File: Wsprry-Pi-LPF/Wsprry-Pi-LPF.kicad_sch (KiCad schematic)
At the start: 13 parts, among them J1 Conn_01x04, J2 Conn_01x04

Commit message: Add 2m LPF values and resolve ERC findings
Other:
- note added: "External equipment supplies GND"
- note added: "VDRN_FEED"
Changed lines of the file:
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@@
+	)
+	(junction
+		(at 105.41 104.14)
+		(diameter 0)
+		(color 0 0 0 0)
 	)
 	(junction
@@
 	(wire
 		(pts
+			(xy 101.6 104.14) (xy 105.41 104.14)
+		)
+		(stroke
+			(width 0)
+			(type default)
+		)
+	)
+	(wire
+		(pts
 			(xy 115.57 90.17) (xy 120.65 90.17)
 		)
@@
 		(pts
 			(xy 135.89 91.44) (xy 135.89 90.17)
-		)
-		(stroke
-			(width 0)
-			(type default)
-		)
-	)
-	(wire
-		(pts
-			(xy 93.98 107.95) (xy 105.41 107.95)
 		)
 		(stroke
@@
 		)
 	)
-	(label "VDRN_FEED"
-		(at 93.98 107.95 0)
+	(text "VDRN_FEED"
+		(exclude_from_sim no)
+		(at 93.98 105.41 0)
 		(effects
 			(font
 				(size 1.27 1.27)
 			)
-			(justify left bottom)
+		)
+	)
+	(text "External equipment supplies GND"
+		(exclude_from_sim no)
+		(at 81.28 100.33 0)
+		(effects
+			(font
+				(size 1.27 1.27)
+			)
 		)
 	)
@@
 					(unit 1)
 				)
+			)
+		)
+	)
+	(symbol
+		(lib_id "Wsprry Pi LPF:PWR_FLAG")
+		(at 101.6 104.14 180)
+		(unit 1)
+		(body_style 1)
+		(exclude_from_sim no)
+		(in_bom yes)
+		(on_board yes)
+		(in_pos_files yes)
+		(dnp no)
+		(property "Reference" "#FLG01"
+			(at 101.6 106.045 0)
+			(show_name no)
+			(do_not_autoplace no)
+			(hide yes)
+			(effects
+				(font
+					(size 1.27 1.27)
+				)
+			)
+		)
+		(property "Value" "PWR_FLAG"
+			(at 101.6 107.95 0)
+			(show_name no)
+			(do_not_autoplace no)
+			(hide yes)
+			(effects
+				(font
+					(size 1.27 1.27)
+				)
+			)
+		)
+		(property "Footprint" ""
+			(at 101.6 104.14 0)
+			(show_name no)
+			(do_not_autoplace no)
+			(hide yes)
+			(effects
+				(font
+					(size 1.27 1.27)
+				)
+			)
+		)
+		(property "Datasheet" ""
+			(at 101.6 104.14 0)
+			(show_name no)
+			(do_not_autoplace no)
+			(hide yes)
+			(effects
+				(font
+					(size 1.27 1.27)
+				)
+			)
+		)
+		(property "Description" "Special symbol for telling ERC where power comes from"
+			(at 101.6 104.14 0)
+			(show_name no)
+			(do_not_autoplace no)
+			(hide yes)
+			(effects
+				(font
+					(size 1.27 1.27)
+				)
+			)
+		)
+		(pin "1"
+		)
+		(instances
+			(project "Wsprry-Pi-LPF"
+				(path "/a5c3480f-f07b-4318-b0ac-3cbcb5b2943e"
+					(reference "#FLG01")
+					(unit 1)
+				)

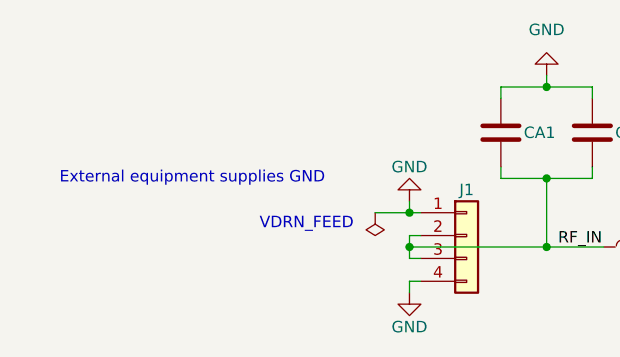
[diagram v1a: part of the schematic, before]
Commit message: Document current LPF validation and 2m values
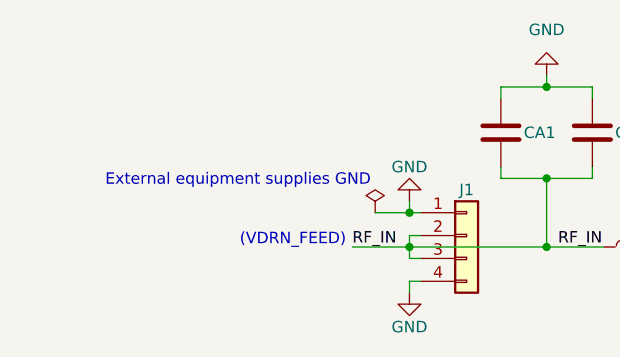
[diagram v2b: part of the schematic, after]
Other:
- note added: "(VDRN_FEED)"
- note removed: "VDRN_FEED"

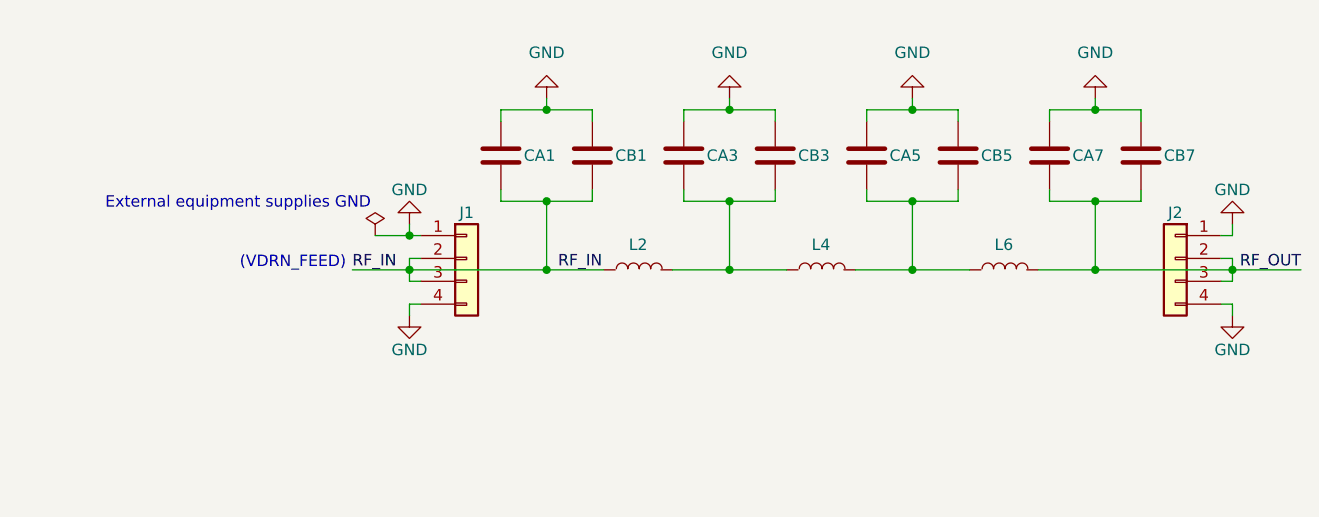
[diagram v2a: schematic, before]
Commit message: Header changed to match QRP Labs
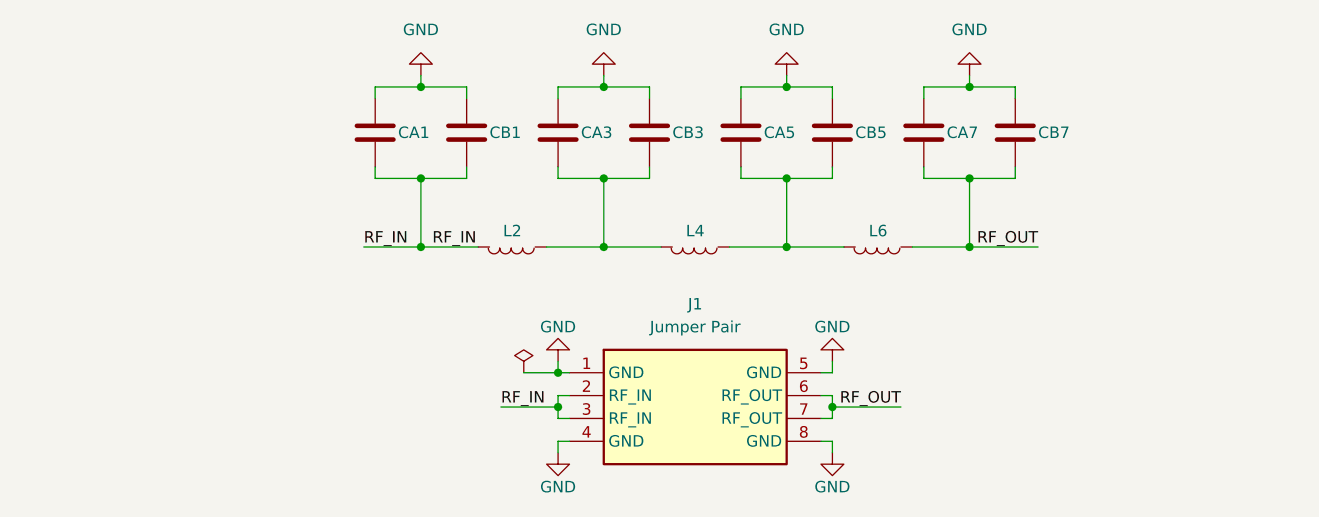
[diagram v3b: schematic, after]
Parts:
- removed J1, J2: Conn_01x04, Wsprry Pi LPF:PinHeader_1x04_P2.54mm_Vertical, symbol Wsprry Pi LPF:Conn_01x04
- added J1: Jumper Pair, Wsprry Pi LPF:LPF_HeaderPair_2x1x04_P2.54mm_S33.02mm, symbol Wsprry Pi LPF:LPF_HeaderPair_2x1x04_P2.54mm_S33.02mm
- renumbered CB7 to CA1, CB1 to CA7, CA7 to CB1, CA1 to CB7, L6 to L2, L2 to L6
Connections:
- net GND: now also J1.1 (GND), J1.4 (GND), J1.5 (GND), J1.8 (GND)
- net RF_IN: now also CA1.2, CB1.2, L2.2, J1.2 (RF_IN), J1.3 (RF_IN); no longer CA7.2, CB7.2, L6.1
- net RF_OUT: now also CA7.2, CB7.2, L6.1, J1.6 (RF_OUT), J1.7 (RF_OUT); no longer CA1.2, CB1.2, L2.2
- net at CA5.2, CB5.2: now also L4.1, L6.2; no longer L2.1, L4.2
- net at CA3.2, CB3.2: now also L2.1, L4.2; no longer L4.1, L6.2
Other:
- note removed: "(VDRN_FEED)"
- note removed: "External equipment supplies GND"
- moved on the sheet: CA1, CA3, CA5, CA7, CB1, CB3, CB5, CB7, L2, L4, L6
